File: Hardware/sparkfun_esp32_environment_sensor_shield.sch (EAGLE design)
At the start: 49 parts, among them J1 WEATHER_METER-WIND, J2 WEATHER_METER-RAIN, U1 BME280, U2 CCS811, U3 TSL2561FN, U4 TVS Diode

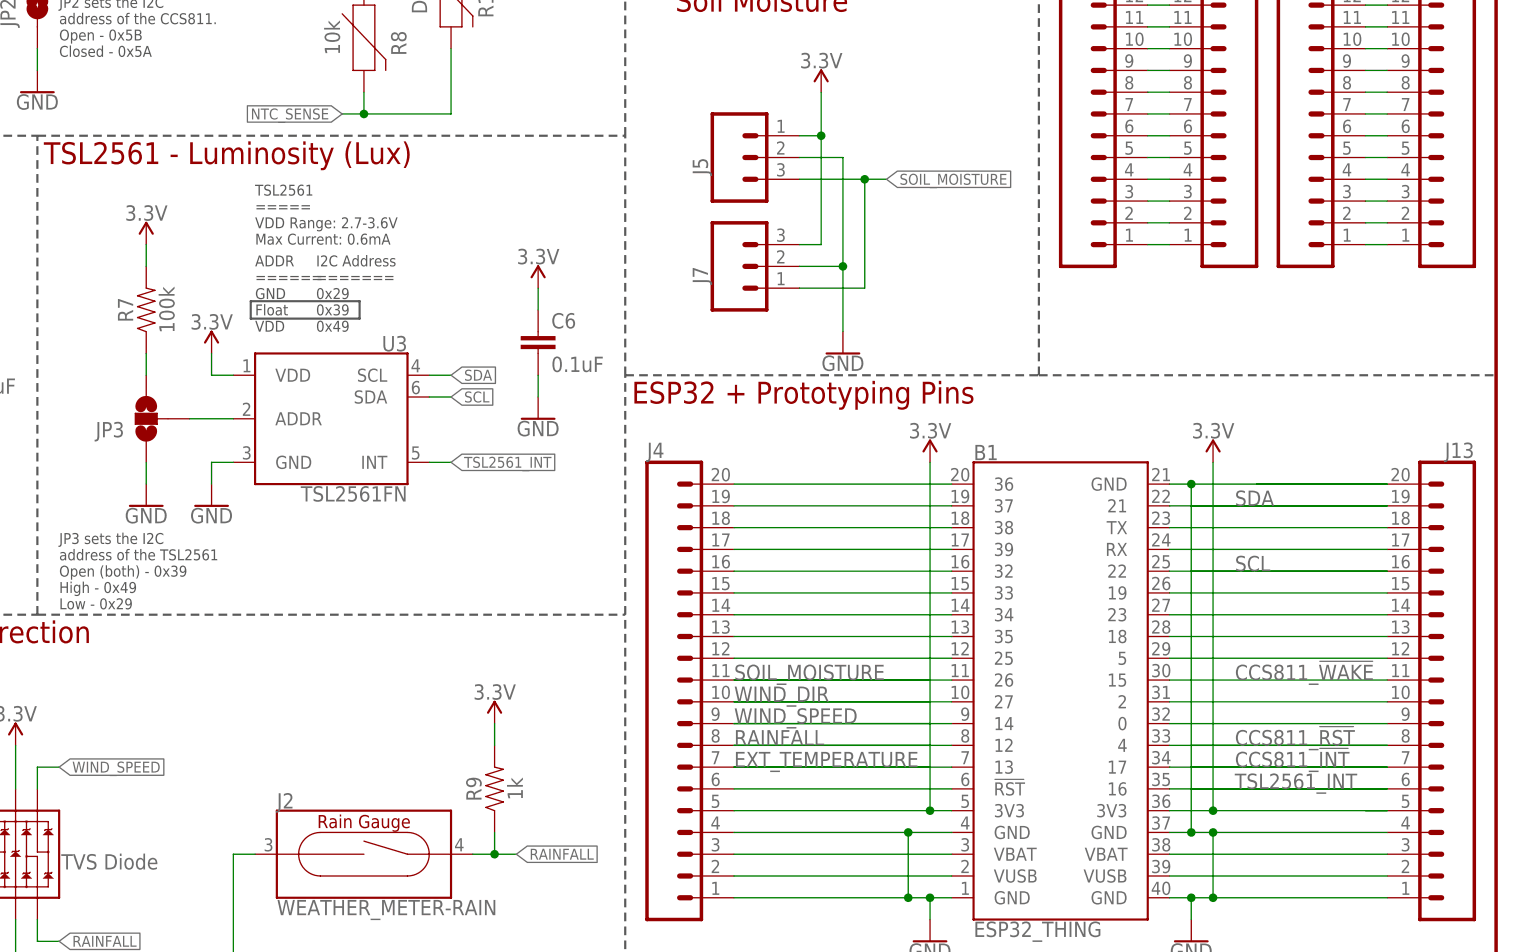
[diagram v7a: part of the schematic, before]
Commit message: Replaced TLS2561 sensor with APDS-9301
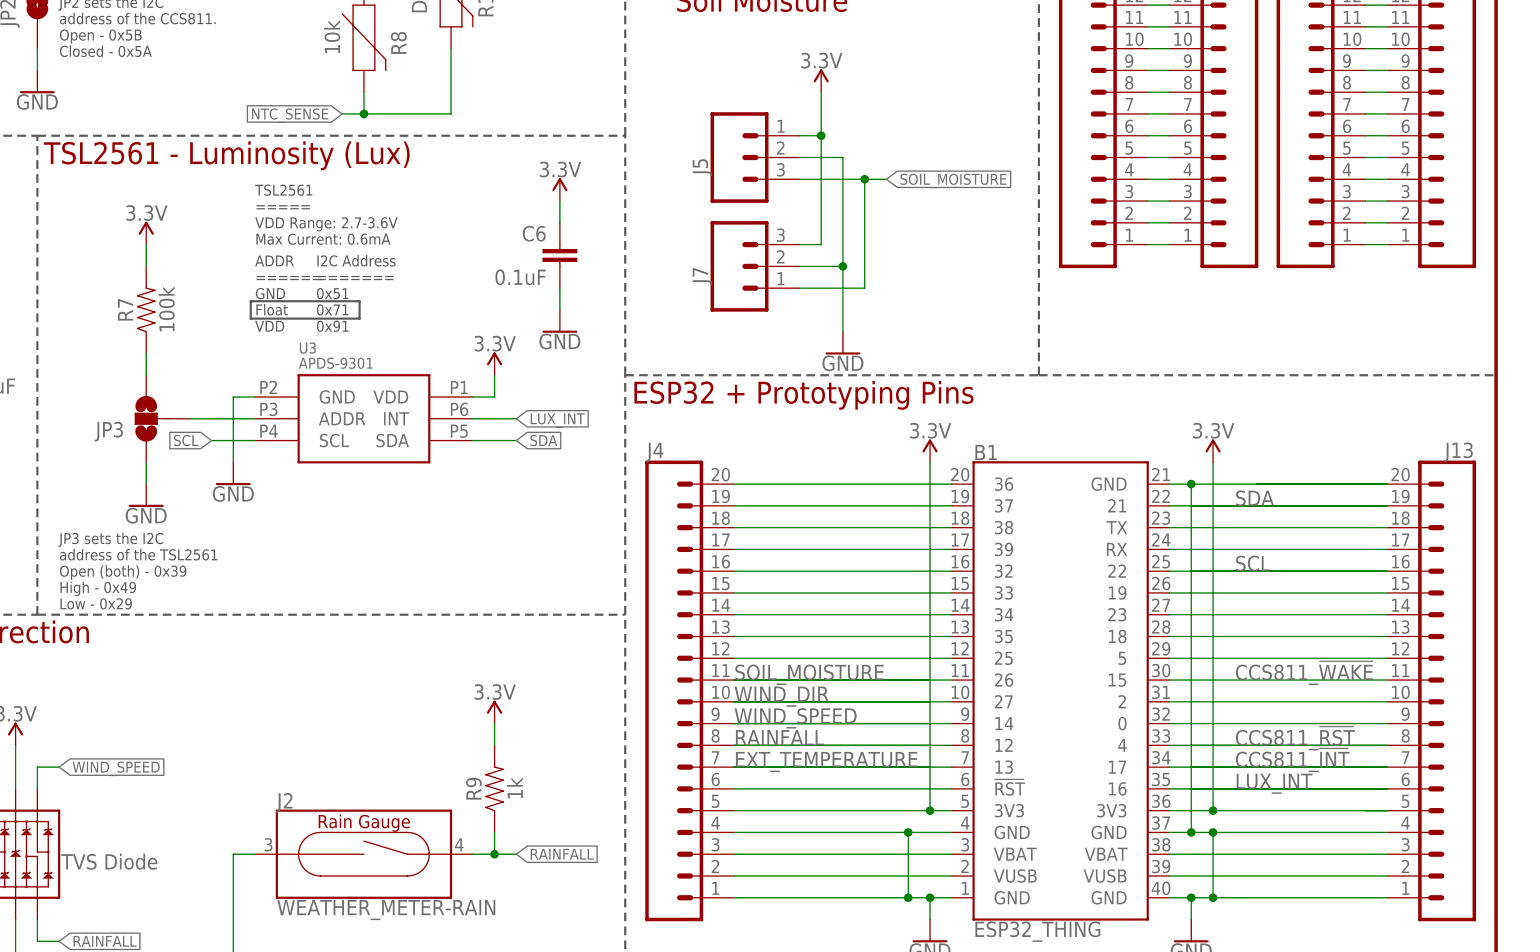
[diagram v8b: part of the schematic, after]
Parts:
- U3: value TSL2561FN -> APDS-9301; device SparkFun-Sensors:TSL2561FN -> SparkFun-Sensors:APDS-9301
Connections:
- net TSL2561_INT renamed LUX_INT
- net SCL: now also U3.SCL; no longer U3.SDA
- net SDA: now also U3.SDA; no longer U3.SCL
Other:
- note added: "I2C Address ======= 0x51 0x71 0x91"
- note removed: "I2C Address ======= 0x29 0x39 0x49"
- moved on the sheet: C6, U3
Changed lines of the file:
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@@
 <part name="GND18" library="SparkFun-PowerSymbols" deviceset="GND" device=""/>
 <part name="SUPPLY21" library="SparkFun-PowerSymbols" deviceset="3.3V" device=""/>
-<part name="U3" library="SparkFun-Sensors" deviceset="TSL2561" device="FN"/>
 <part name="U1" library="SparkFun-Sensors" deviceset="BME280" device="" value="BME280"/>
 <part name="GND1" library="SparkFun-PowerSymbols" deviceset="GND" device=""/>
@@
 <part name="GND7" library="SparkFun-PowerSymbols" deviceset="GND" device=""/>
 <part name="LOGO3" library="SparkFun-Aesthetics" deviceset="SFE_LOGO_FLAME" device=".1_INCH"/>
+<part name="U3" library="SparkFun-Sensors" deviceset="APDS-9301" device="" value="APDS-9301"/>
 </parts>
 <sheets>
@@
 <text x="111.252" y="109.22" size="1.27" layer="97">I2C Address
 =======
-0x29
-0x39
-0x49</text>
+0x51
+0x71
+0x91</text>
 <text x="15.24" y="111.76" size="1.27" layer="97">BME280
 =====
@@
 <instance part="GND18" gate="1" x="185.42" y="157.48"/>
 <instance part="SUPPLY21" gate="G$1" x="185.42" y="175.26"/>
-<instance part="U3" gate="G$1" x="114.3" y="99.06" rot="MR0"/>
 <instance part="U1" gate="U1" x="20.32" y="93.98"/>
 <instance part="GND1" gate="1" x="5.08" y="81.28"/>
-<instance part="GND12" gate="1" x="99.06" y="88.9"/>
+<instance part="GND12" gate="1" x="101.6" y="91.44"/>
 <instance part="JP3" gate="G$1" x="91.44" y="99.06" rot="R180"/>
 <instance part="SUPPLY12" gate="G$1" x="91.44" y="119.38"/>
 <instance part="GND11" gate="1" x="91.44" y="88.9"/>
-<instance part="SUPPLY13" gate="G$1" x="99.06" y="106.68"/>
+<instance part="SUPPLY13" gate="G$1" x="132.08" y="104.14"/>
 <instance part="R13" gate="G$1" x="149.86" y="160.02" rot="R90"/>
 <instance part="R14" gate="G$1" x="165.1" y="160.02" rot="R90"/>
 <instance part="SUPPLY18" gate="G$1" x="157.48" y="177.8"/>
-<instance part="C6" gate="G$1" x="137.16" y="106.68"/>
-<instance part="SUPPLY17" gate="G$1" x="137.16" y="114.3"/>
-<instance part="GND15" gate="1" x="137.16" y="99.06"/>
+<instance part="C6" gate="G$1" x="139.7" y="116.84" rot="MR0"/>
+<instance part="SUPPLY17" gate="G$1" x="139.7" y="124.46"/>
+<instance part="GND15" gate="1" x="139.7" y="109.22"/>
 <instance part="SUPPLY1" gate="G$1" x="5.08" y="101.6"/>
 <instance part="R7" gate="G$1" x="91.44" y="111.76" rot="R90"/>
@@
 <instance part="GND7" gate="1" x="76.2" y="33.02" rot="MR0"/>
 <instance part="LOGO3" gate="G$1" x="33.782" y="12.446"/>
+<instance part="U3" gate="G$1" x="116.84" y="99.06"/>
 </instances>
 <busses>
@@
 </segment>
 <segment>
-<pinref part="GND12" gate="1" pin="GND"/>
-<wire x1="99.06" y1="91.44" x2="99.06" y2="93.98" width="0.1524" layer="91"/>
-<pinref part="U3" gate="G$1" pin="GND"/>
-<wire x1="99.06" y1="93.98" x2="101.6" y2="93.98" width="0.1524" layer="91"/>
-</segment>
-<segment>
 <pinref part="JP3" gate="G$1" pin="1"/>
 <pinref part="GND11" gate="1" pin="GND"/>
@@
 <pinref part="C6" gate="G$1" pin="2"/>
 <pinref part="GND15" gate="1" pin="GND"/>
-<wire x1="137.16" y1="101.6" x2="137.16" y2="104.14" width="0.1524" layer="91"/>
+<wire x1="139.7" y1="111.76" x2="139.7" y2="114.3" width="0.1524" layer="91"/>
 </segment>
 <segment>
@@
 <junction x="215.9" y="50.8"/>
 </segment>
+<segment>
+<pinref part="GND12" gate="1" pin="GND"/>
+<wire x1="101.6" y1="93.98" x2="101.6" y2="101.6" width="0.1524" layer="91"/>
+<pinref part="U3" gate="G$1" pin="GND"/>
+<wire x1="101.6" y1="101.6" x2="104.14" y2="101.6" width="0.1524" layer="91"/>
+</segment>
 </net>
 <net name="SCL" class="0">
@@
 </segment>
 <segment>
-<pinref part="U3" gate="G$1" pin="SDA"/>
-<wire x1="124.46" y1="101.6" x2="127" y2="101.6" width="0.1524" layer="91"/>
-<label x="127" y="101.6" size="1.27" layer="95" xref="yes"/>
+<wire x1="104.14" y1="96.52" x2="99.06" y2="96.52" width="0.1524" layer="91"/>
+<label x="99.06" y="96.52" size="1.27" layer="95" rot="R180" xref="yes"/>
+<pinref part="U3" gate="G$1" pin="SCL"/>
 </segment>
 <segment>
@@
 </segment>
 <segment>
-<pinref part="U3" gate="G$1" pin="SCL"/>
-<wire x1="124.46" y1="104.14" x2="127" y2="104.14" width="0.1524" layer="91"/>
-<label x="127" y="104.14" size="1.27" layer="95" xref="yes"/>
+<wire x1="129.54" y1="96.52" x2="134.62" y2="96.52" width="0.1524" layer="91"/>
+<label x="134.62" y="96.52" size="1.27" layer="95" xref="yes"/>
+<pinref part="U3" gate="G$1" pin="SDA"/>
 </segment>
 <segment>
@@
 </segment>
 <segment>
-<pinref part="SUPPLY13" gate="G$1" pin="3.3V"/>
-<wire x1="99.06" y1="104.14" x2="99.06" y2="106.68" width="0.1524" layer="91"/>
-<pinref part="U3" gate="G$1" pin="VDD"/>
-<wire x1="101.6" y1="104.14" x2="99.06" y2="104.14" width="0.1524" layer="91"/>
-</segment>
-<segment>
 <pinref part="C6" gate="G$1" pin="1"/>
 <pinref part="SUPPLY17" gate="G$1" pin="3.3V"/>
-<wire x1="137.16" y1="114.3" x2="137.16" y2="111.76" width="0.1524" layer="91"/>
+<wire x1="139.7" y1="124.46" x2="139.7" y2="121.92" width="0.1524" layer="91"/>
 </segment>
 <segment>
@@
 <wire x1="76.2" y1="60.96" x2="76.2" y2="55.88" width="0.1524" layer="91"/>
 </segment>
+<segment>
+<pinref part="U3" gate="G$1" pin="VDD"/>
+<pinref part="SUPPLY13" gate="G$1" pin="3.3V"/>
+<wire x1="129.54" y1="101.6" x2="132.08" y2="101.6" width="0.1524" layer="91"/>
+<wire x1="132.08" y1="101.6" x2="132.08" y2="104.14" width="0.1524" layer="91"/>
+</segment>
 </net>
 <net name="ADDR_TSL2561" class="0">
 <segment>
+<pinref part="JP3" gate="G$1" pin="2"/>
+<wire x1="104.14" y1="99.06" x2="96.52" y2="99.06" width="0.1524" layer="91"/>
 <pinref part="U3" gate="G$1" pin="ADDR"/>
-<pinref part="JP3" gate="G$1" pin="2"/>
-<wire x1="101.6" y1="99.06" x2="96.52" y2="99.06" width="0.1524" layer="91"/>
 </segment>
 </net>
-<net name="TSL2561_INT" class="0">
-<segment>
+<net name="LUX_INT" class="0">
+<segment>
+<label x="134.62" y="99.06" size="1.27" layer="95" xref="yes"/>
 <pinref part="U3" gate="G$1" pin="INT"/>
-<wire x1="124.46" y1="93.98" x2="127" y2="93.98" width="0.1524" layer="91"/>
-<label x="127" y="93.98" size="1.27" layer="95" xref="yes"/>
-</segment>
-<segment>
+<wire x1="134.62" y1="99.06" x2="129.54" y2="99.06" width="0.1524" layer="91"/>
+</segment>
+<segment>
